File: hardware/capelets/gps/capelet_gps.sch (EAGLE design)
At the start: 8 parts, among them IC1 SAM-M8Q, P1 SHPRD_CPLT_G, T1 SI2374DSSOT23-VSHAY

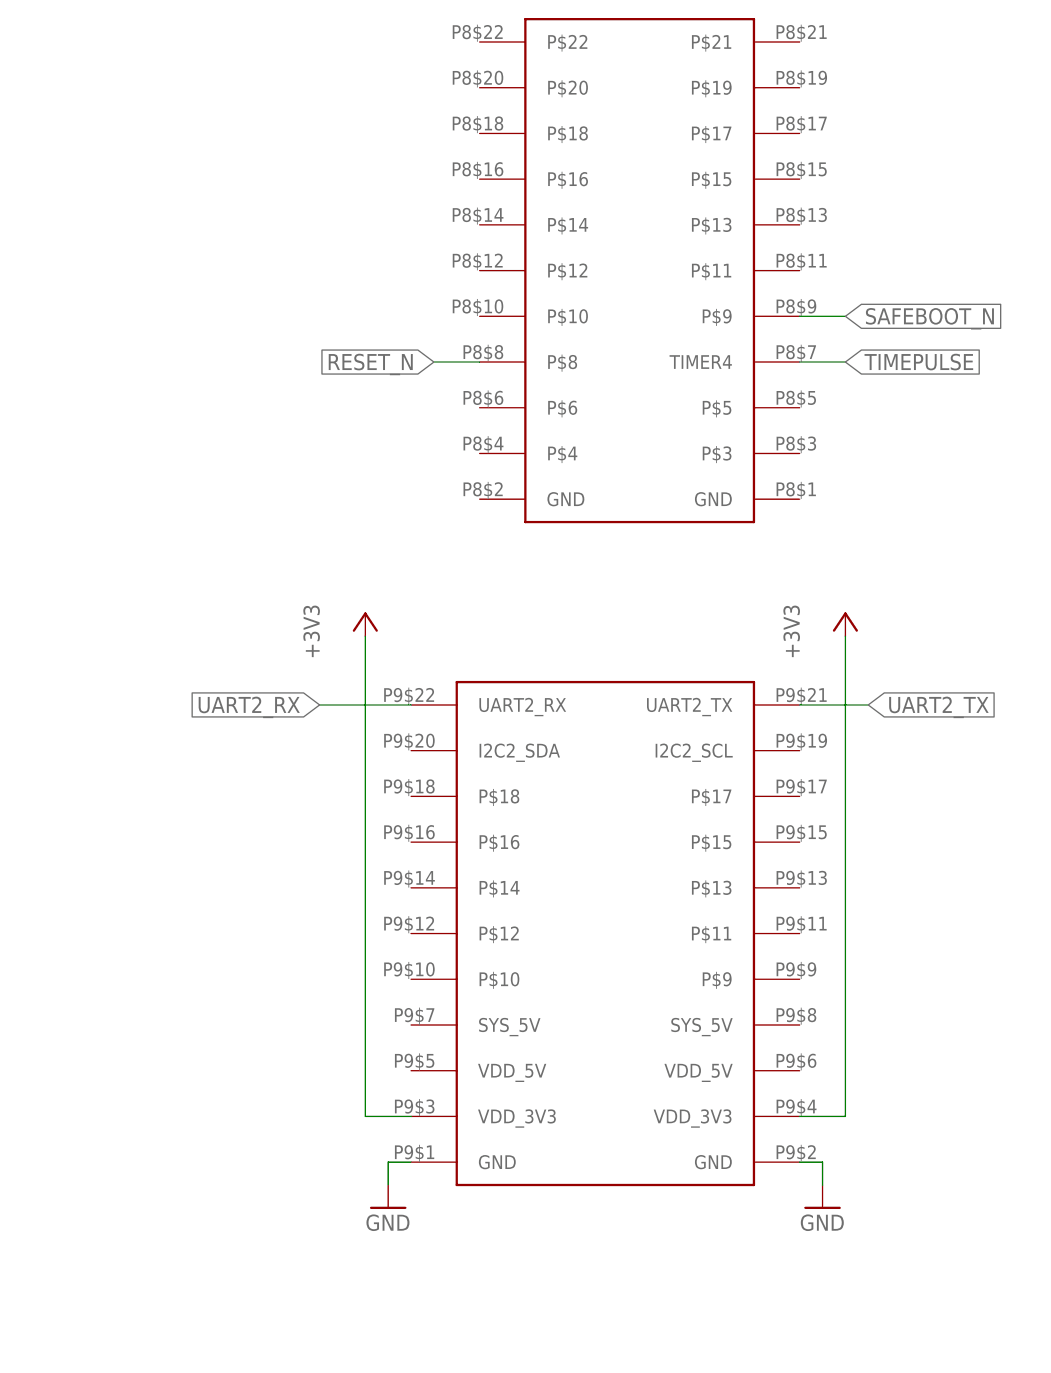
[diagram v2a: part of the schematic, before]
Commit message: hardware: prepared GPS capelet for professional assembly
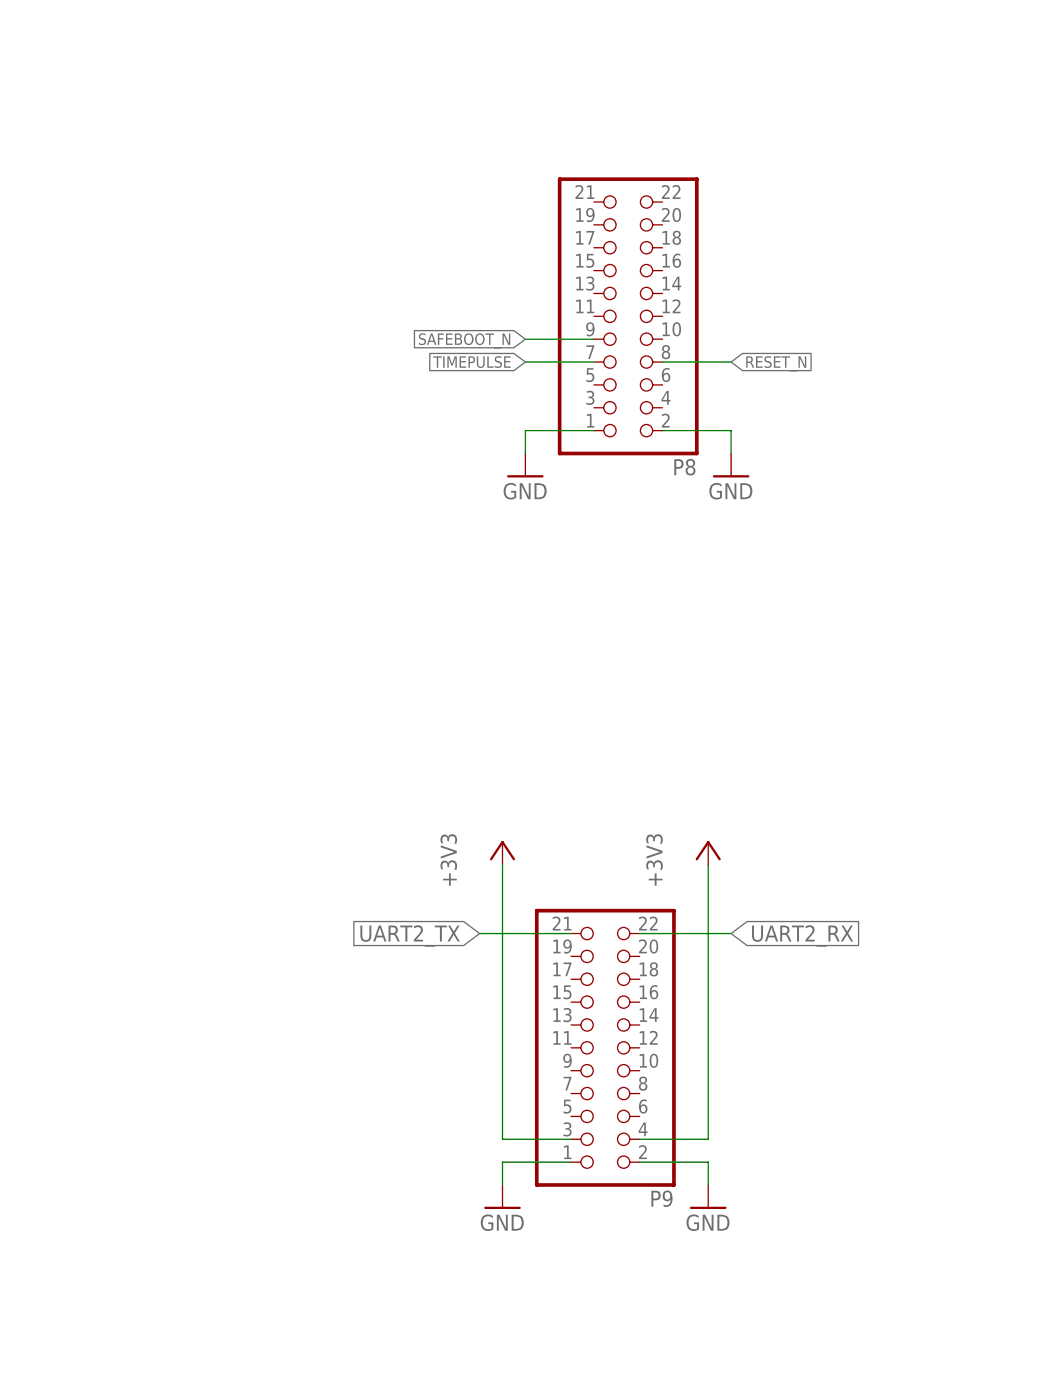
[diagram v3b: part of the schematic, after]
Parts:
- removed P1: SHPRD_CPLT_G, shepherd:SHPRD_CPLT_G
- added P8, P9: (no value), shepherd:PINHD-2X11
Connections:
- net +3V3: now also P9.3, P9.4; no longer P1G$3.VDD_3V3@1, P1G$3.VDD_3V3@2
- net GND: now also P8.1, P8.2, P9.1, P9.2; no longer P1G$3.GND@1, P1G$3.GND@2
- net RESET_N: now also P8.7; no longer P1G$2.P$8
- net SAFEBOOT_N: now also P8.10; no longer P1G$2.P$9
- net TIMEPULSE: now also P8.8; no longer P1G$2.TIMER4
- net UART2_RX: now also P9.21; no longer P1G$3.UART2_RX
- net UART2_TX: now also P9.22; no longer P1G$3.UART2_TX
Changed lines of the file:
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@@
 <parts>
 <part name="IC1" library="shepherd" deviceset="SAM-M8Q" device=""/>
-<part name="P1" library="shepherd" deviceset="SHPRD_CPLT_G" device=""/>
 <part name="+3V1" library="supply1" library_urn="urn:adsk.eagle:library:371" deviceset="+3V3" device=""/>
 <part name="GND1" library="supply1" library_urn="urn:adsk.eagle:library:371" deviceset="GND" device=""/>
@@
 <part name="C3" library="shepherd" deviceset="C_SMD" device="0805" package3d_urn="urn:adsk.eagle:package:4930364/1" value="0.1u"/>
 <part name="FRAME1" library="frames" library_urn="urn:adsk.eagle:library:229" deviceset="A4L-LOC" device=""/>
+<part name="GND5" library="supply1" library_urn="urn:adsk.eagle:library:371" deviceset="GND" device=""/>
+<part name="GND6" library="supply1" library_urn="urn:adsk.eagle:library:371" deviceset="GND" device=""/>
+<part name="P8" library="shepherd" deviceset="PINHD-2X11" device="" package3d_urn="urn:adsk.eagle:package:22419/2"/>
+<part name="P9" library="shepherd" deviceset="PINHD-2X11" device="" package3d_urn="urn:adsk.eagle:package:22419/2"/>
 </parts>
 <sheets>
@@
 <instances>
 <instance part="IC1" gate="G$1" x="58.42" y="106.68" smashed="yes"/>
-<instance part="P1" gate="G$2" x="200.66" y="111.76" smashed="yes"/>
-<instance part="P1" gate="G$3" x="193.04" y="38.1" smashed="yes"/>
 <instance part="+3V1" gate="G$1" x="50.8" y="152.4" smashed="yes">
 <attribute name="VALUE" x="48.26" y="147.32" size="1.778" layer="96" rot="R90"/>
@@
 <attribute name="VALUE" x="48.26" y="88.9" size="1.778" layer="96"/>
 </instance>
-<instance part="+3V2" gate="G$1" x="182.88" y="101.6" smashed="yes">
-<attribute name="VALUE" x="177.8" y="96.52" size="1.778" layer="96" rot="R90"/>
-</instance>
-<instance part="+3V3" gate="G$1" x="236.22" y="101.6" smashed="yes">
-<attribute name="VALUE" x="231.14" y="96.52" size="1.778" layer="96" rot="R90"/>
-</instance>
-<instance part="GND2" gate="1" x="233.68" y="35.56" smashed="yes">
-<attribute name="VALUE" x="231.14" y="33.02" size="1.778" layer="96"/>
-</instance>
-<instance part="GND3" gate="1" x="185.42" y="35.56" smashed="yes">
-<attribute name="VALUE" x="182.88" y="33.02" size="1.778" layer="96"/>
+<instance part="+3V2" gate="G$1" x="198.12" y="76.2" smashed="yes">
+<attribute name="VALUE" x="193.04" y="71.12" size="1.778" layer="96" rot="R90"/>
+</instance>
+<instance part="+3V3" gate="G$1" x="220.98" y="76.2" smashed="yes">
+<attribute name="VALUE" x="215.9" y="71.12" size="1.778" layer="96" rot="R90"/>
+</instance>
+<instance part="GND2" gate="1" x="220.98" y="35.56" smashed="yes">
+<attribute name="VALUE" x="218.44" y="33.02" size="1.778" layer="96"/>
+</instance>
+<instance part="GND3" gate="1" x="198.12" y="35.56" smashed="yes">
+<attribute name="VALUE" x="195.58" y="33.02" size="1.778" layer="96"/>
 </instance>
 <instance part="T1" gate="G$1" x="104.14" y="35.56" smashed="yes">
@@
 <attribute name="LAST_DATE_TIME" x="217.17" y="10.16" size="2.286" layer="94"/>
 <attribute name="SHEET" x="230.505" y="5.08" size="2.54" layer="94"/>
+</instance>
+<instance part="GND5" gate="1" x="223.52" y="116.84" smashed="yes">
+<attribute name="VALUE" x="220.98" y="114.3" size="1.778" layer="96"/>
+</instance>
+<instance part="GND6" gate="1" x="200.66" y="116.84" smashed="yes">
+<attribute name="VALUE" x="198.12" y="114.3" size="1.778" layer="96"/>
+</instance>
+<instance part="P8" gate="A" x="213.36" y="134.62" smashed="yes" rot="R180">
+<attribute name="NAME" x="219.71" y="118.745" size="1.778" layer="95" rot="R180"/>
+<attribute name="VALUE" x="219.71" y="152.4" size="1.778" layer="96" rot="R180"/>
+</instance>
+<instance part="P9" gate="A" x="210.82" y="53.34" smashed="yes" rot="R180">
+<attribute name="NAME" x="217.17" y="37.465" size="1.778" layer="95" rot="R180"/>
+<attribute name="VALUE" x="217.17" y="71.12" size="1.778" layer="96" rot="R180"/>
 </instance>
 </instances>
@@
 </segment>
 <segment>
-<pinref part="+3V2" gate="G$1" pin="+3V3"/>
-<pinref part="P1" gate="G$3" pin="VDD_3V3@1"/>
-<wire x1="182.88" y1="99.06" x2="182.88" y2="45.72" width="0.1524" layer="91"/>
-<wire x1="182.88" y1="45.72" x2="187.96" y2="45.72" width="0.1524" layer="91"/>
-</segment>
-<segment>
-<pinref part="P1" gate="G$3" pin="VDD_3V3@2"/>
-<pinref part="+3V3" gate="G$1" pin="+3V3"/>
-<wire x1="231.14" y1="45.72" x2="236.22" y2="45.72" width="0.1524" layer="91"/>
-<wire x1="236.22" y1="45.72" x2="236.22" y2="99.06" width="0.1524" layer="91"/>
-</segment>
-<segment>
 <pinref part="R1" gate="G$1" pin="2"/>
 <pinref part="+3V4" gate="G$1" pin="+3V3"/>
 <wire x1="106.68" y1="63.5" x2="106.68" y2="66.04" width="0.1524" layer="91"/>
+</segment>
+<segment>
+<pinref part="+3V2" gate="G$1" pin="+3V3"/>
+<wire x1="198.12" y1="43.18" x2="198.12" y2="73.66" width="0.1524" layer="91"/>
+<pinref part="P9" gate="A" pin="4"/>
+<wire x1="198.12" y1="43.18" x2="205.74" y2="43.18" width="0.1524" layer="91"/>
+</segment>
+<segment>
+<pinref part="+3V3" gate="G$1" pin="+3V3"/>
+<wire x1="220.98" y1="43.18" x2="220.98" y2="73.66" width="0.1524" layer="91"/>
+<pinref part="P9" gate="A" pin="3"/>
+<wire x1="220.98" y1="43.18" x2="213.36" y2="43.18" width="0.1524" layer="91"/>
 </segment>
 </net>
@@
 <segment>
 <pinref part="GND3" gate="1" pin="GND"/>
-<pinref part="P1" gate="G$3" pin="GND@1"/>
-<wire x1="185.42" y1="38.1" x2="185.42" y2="40.64" width="0.1524" layer="91"/>
-<wire x1="185.42" y1="40.64" x2="187.96" y2="40.64" width="0.1524" layer="91"/>
-</segment>
-<segment>
-<pinref part="P1" gate="G$3" pin="GND@2"/>
+<wire x1="198.12" y1="38.1" x2="198.12" y2="40.64" width="0.1524" layer="91"/>
+<pinref part="P9" gate="A" pin="2"/>
+<wire x1="198.12" y1="40.64" x2="205.74" y2="40.64" width="0.1524" layer="91"/>
+</segment>
+<segment>
 <pinref part="GND2" gate="1" pin="GND"/>
-<wire x1="231.14" y1="40.64" x2="233.68" y2="40.64" width="0.1524" layer="91"/>
-<wire x1="233.68" y1="40.64" x2="233.68" y2="38.1" width="0.1524" layer="91"/>
+<wire x1="220.98" y1="40.64" x2="220.98" y2="38.1" width="0.1524" layer="91"/>
+<pinref part="P9" gate="A" pin="1"/>
+<wire x1="220.98" y1="40.64" x2="213.36" y2="40.64" width="0.1524" layer="91"/>
 </segment>
 <segment>
@@
 <wire x1="106.68" y1="25.4" x2="106.68" y2="30.48" width="0.1524" layer="91"/>
 </segment>
+<segment>
+<pinref part="GND6" gate="1" pin="GND"/>
+<wire x1="200.66" y1="119.38" x2="200.66" y2="121.92" width="0.1524" layer="91"/>
+<pinref part="P8" gate="A" pin="2"/>
+<wire x1="200.66" y1="121.92" x2="208.28" y2="121.92" width="0.1524" layer="91"/>
+</segment>
+<segment>
+<pinref part="GND5" gate="1" pin="GND"/>
+<wire x1="223.52" y1="121.92" x2="223.52" y2="119.38" width="0.1524" layer="91"/>
+<pinref part="P8" gate="A" pin="1"/>
+<wire x1="223.52" y1="121.92" x2="215.9" y2="121.92" width="0.1524" layer="91"/>
+</segment>
 </net>
 <net name="UART2_TX" class="0">
@@
 </segment>
 <segment>
-<pinref part="P1" gate="G$3" pin="UART2_TX"/>
-<wire x1="231.14" y1="91.44" x2="238.76" y2="91.44" width="0.1524" layer="91"/>
-<label x="238.76" y="91.44" size="1.778" layer="95" xref="yes"/>
+<label x="195.58" y="66.04" size="1.778" layer="95" rot="R180" xref="yes"/>
+<pinref part="P9" gate="A" pin="22"/>
+<wire x1="195.58" y1="66.04" x2="205.74" y2="66.04" width="0.1524" layer="91"/>
 </segment>
 </net>
@@
 </segment>
 <segment>
-<pinref part="P1" gate="G$3" pin="UART2_RX"/>
-<wire x1="187.96" y1="91.44" x2="177.8" y2="91.44" width="0.1524" layer="91"/>
-<label x="177.8" y="91.44" size="1.778" layer="95" rot="R180" xref="yes"/>
+<label x="223.52" y="66.04" size="1.778" layer="95" xref="yes"/>
+<pinref part="P9" gate="A" pin="21"/>
+<wire x1="223.52" y1="66.04" x2="213.36" y2="66.04" width="0.1524" layer="91"/>
 </segment>
 </net>
@@
 </segment>
 <segment>
-<pinref part="P1" gate="G$2" pin="TIMER4"/>
-<wire x1="231.14" y1="129.54" x2="236.22" y2="129.54" width="0.1524" layer="91"/>
-<label x="236.22" y="129.54" size="1.778" layer="95" xref="yes"/>
+<wire x1="208.28" y1="129.54" x2="200.66" y2="129.54" width="0.1524" layer="91"/>
+<label x="200.66" y="129.54" size="1.27" layer="95" rot="R180" xref="yes"/>
+<pinref part="P8" gate="A" pin="8"/>
 </segment>
 </net>
@@
 </segment>
 <segment>
-<pinref part="P1" gate="G$2" pin="P$8"/>
-<wire x1="195.58" y1="129.54" x2="190.5" y2="129.54" width="0.1524" layer="91"/>
-<label x="190.5" y="129.54" size="1.778" layer="95" rot="R180" xref="yes"/>
+<wire x1="215.9" y1="129.54" x2="223.52" y2="129.54" width="0.1524" layer="91"/>
+<label x="223.52" y="129.54" size="1.27" layer="95" xref="yes"/>
+<pinref part="P8" gate="A" pin="7"/>
 </segment>
 </net>
@@
 </segment>
 <segment>
-<pinref part="P1" gate="G$2" pin="P$9"/>
-<wire x1="231.14" y1="134.62" x2="236.22" y2="134.62" width="0.1524" layer="91"/>
-<label x="236.22" y="134.62" size="1.778" layer="95" xref="yes"/>
-</segment>
-</net>
+<wire x1="208.28" y1="132.08" x2="200.66" y2="132.08" width="0.1524" layer="91"/>
+<label x="200.66" y="132.08" size="1.27" layer="95" rot="R180" xref="yes"/>
+<pinref part="P8" gate="A" pin="10"/>
+</segment>
+</net>
